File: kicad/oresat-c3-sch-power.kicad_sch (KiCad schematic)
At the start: 67 parts, among them U31 LP2985AIM5-3.3, U34 TPS259621DDA, U35 TPS259620DDA, U36 LTC3624-5, U38 LP2985AIM5-3.3, U6 LTC3624-5

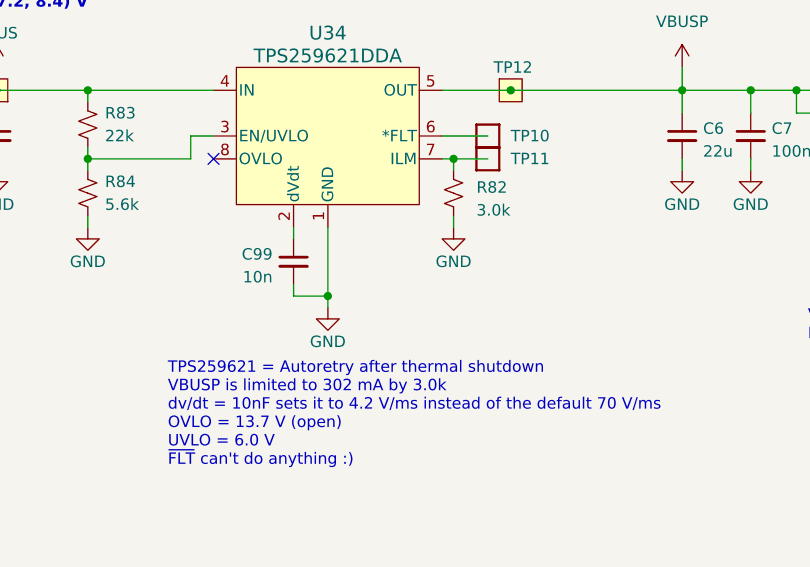
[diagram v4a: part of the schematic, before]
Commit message: Fixed R82 so that the damn thing doesn't reboot every two seconds. Fixed R63 to extend the watchdog timer. Fixed R83 and R84 in order to set the UVLO correctly.
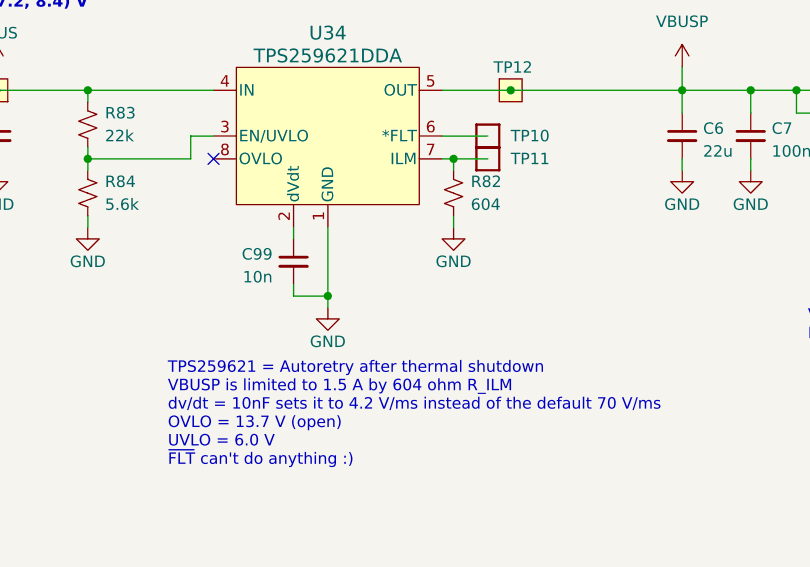
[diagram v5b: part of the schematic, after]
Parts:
- R82: value 3.0k -> 604
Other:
- note added: "TPS259621 = Autoretry after thermal shutdown VBUSP is limited to 1.5 A by 604 ohm R_ILM dv/dt = 10nF sets it to 4.2 V/ms instead of the default 70 V/ms OVLO = 13.7 V (open) UVLO = 6.0 V ~{FLT} can't do anything :)"
- note removed: "TPS259621 = Autoretry after thermal shutdown VBUSP is limited to 302 mA by 3.0k dv/dt = 10nF sets it to 4.2 V/ms instead of the default 70 V/ms OVLO = 13.7 V (open) UVLO = 6.0 V ~{FLT} can't do anything :)"
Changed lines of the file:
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@@
     (effects (font (size 1.27 1.27)) (justify left bottom))
   )
-  (text "TPS259621 = Autoretry after thermal shutdown\nVBUSP is limited to 302 mA by 3.0k\ndv/dt = 10nF sets it to 4.2 V/ms instead of the default 70 V/ms\nOVLO = 13.7 V (open)\nUVLO = 6.0 V\n~{FLT} can't do anything :)"
+  (text "TPS259621 = Autoretry after thermal shutdown\nVBUSP is limited to 1.5 A by 604 ohm R_ILM\ndv/dt = 10nF sets it to 4.2 V/ms instead of the default 70 V/ms\nOVLO = 13.7 V (open)\nUVLO = 6.0 V\n~{FLT} can't do anything :)"
     (at 132.715 114.3 0)
     (effects (font (size 1.27 1.27)) (justify left bottom))
@@
   (symbol (lib_id "Device:R_Small_US") (at 164.465 83.82 0) (unit 1)
     (in_bom yes) (on_board yes) (dnp no) (fields_autoplaced)
-    (property "Reference" "R82" (at 167.005 83.185 0)
-      (effects (font (size 1.27 1.27)) (justify left))
-    )
-    (property "Value" "3.0k" (at 167.005 85.725 0)
-      (effects (font (size 1.27 1.27)) (justify left))
-    )
+    (property "Reference" "R82" (at 166.37 82.55 0)
+      (effects (font (size 1.27 1.27)) (justify left))
+    )
+    (property "Value" "604" (at 166.37 85.09 0)
+      (effects (font (size 1.27 1.27)) (justify left))
+    )

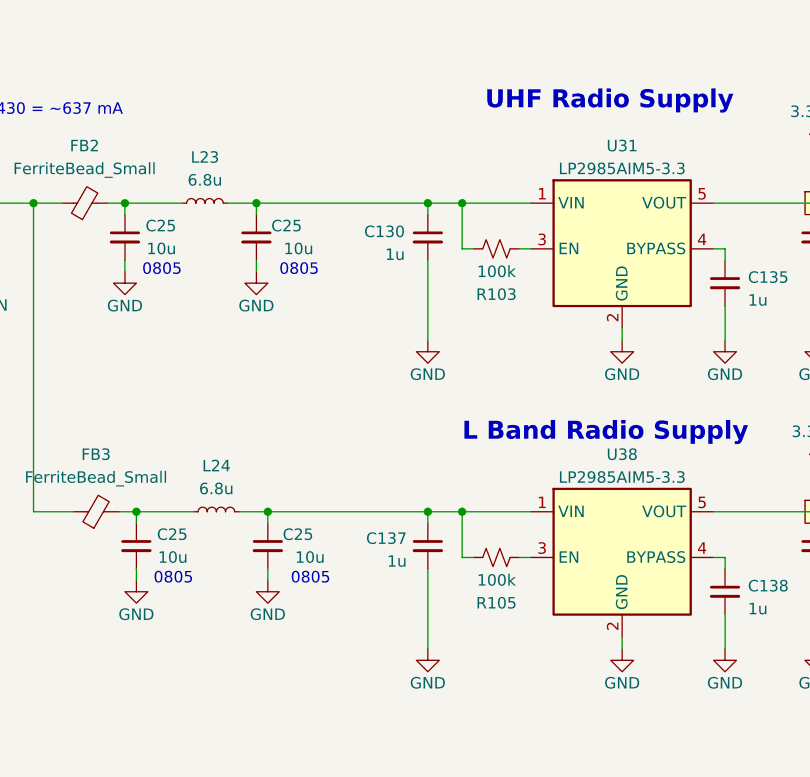
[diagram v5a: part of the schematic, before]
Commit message: changed R values, connected radio enables, more 6.1 implementations
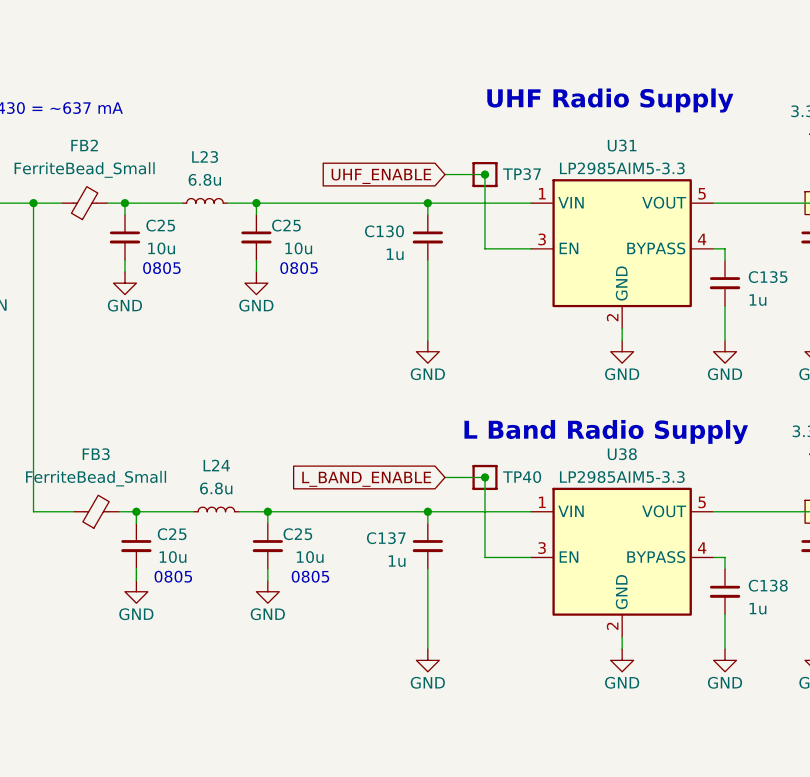
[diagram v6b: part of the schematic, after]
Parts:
- removed R103, R105: 100k, Resistor_SMD:R_0603_1608Metric, symbol Device:R_Small_US
- added TP37, TP40: Test-Point, oresat-misc:TestPoint_Pad_D1.0mm, symbol oresat-misc:Test-Point-1mm-round
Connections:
- net UHF_ENABLE: now reaches U31.3 (EN)
- net UHF_ENABLE: now also TP37.1
- net L_BAND_ENABLE: now reaches U38.3 (EN)
- net L_BAND_ENABLE: now also TP40.1
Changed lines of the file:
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@@
     (title "OreSat C3: Power")
     (date "2023-05-29")
-    (rev "6.0")
+    (rev "6.1")
   )
   (junction (at 349.25 152.4) (diameter 0) (color 0 0 0 0)
@@
   (junction (at 126.365 157.48) (diameter 0) (color 0 0 0 0)
   )
+  (junction (at 312.42 182.88) (diameter 0) (color 0 0 0 0)
+  )
+  (junction (at 312.42 149.225) (diameter 0) (color 0 0 0 0)
+  )
   (junction (at 254.635 72.39) (diameter 0) (color 0 0 0 0)
   )
@@
   (junction (at 349.25 186.69) (diameter 0) (color 0 0 0 0)
   )
-  (junction (at 309.88 186.69) (diameter 0) (color 0 0 0 0)
-  )
   (junction (at 272.415 152.4) (diameter 0) (color 0 0 0 0)
   )
@@
   (junction (at 250.825 152.4) (diameter 0) (color 0 0 0 0)
   )
-  (junction (at 309.88 152.4) (diameter 0) (color 0 0 0 0)
-  )
   (junction (at 113.665 72.39) (diameter 0) (color 0 0 0 0)
   )
@@
     (stroke (width 0) (type default))
   )
+  (wire (pts (xy 307.975 182.88) (xy 312.42 182.88))
+    (stroke (width 0) (type default))
+  )
   (wire (pts (xy 150.495 87.63) (xy 150.495 95.25))
     (stroke (width 0) (type default))
@@
     (stroke (width 0) (type default))
   )
-  (wire (pts (xy 309.88 191.77) (xy 311.15 191.77))
-    (stroke (width 0) (type default))
-  )
   (wire (pts (xy 272.415 80.01) (xy 272.415 82.55))
     (stroke (width 0) (type default))
@@
     (stroke (width 0) (type default))
   )
-  (wire (pts (xy 309.88 186.69) (xy 309.88 191.77))
-    (stroke (width 0) (type default))
-  )
   (wire (pts (xy 75.565 157.48) (xy 79.375 157.48))
     (stroke (width 0) (type default))
@@
     (stroke (width 0) (type default))
   )
-  (wire (pts (xy 309.88 152.4) (xy 306.07 152.4))
-    (stroke (width 0) (type default))
-  )
   (wire (pts (xy 75.565 175.26) (xy 75.565 176.53))
     (stroke (width 0) (type default))
@@
     (stroke (width 0) (type default))
   )
+  (wire (pts (xy 312.42 191.77) (xy 312.42 182.88))
+    (stroke (width 0) (type default))
+  )
   (wire (pts (xy 177.165 152.4) (xy 174.625 152.4))
     (stroke (width 0) (type default))
@@
     (stroke (width 0) (type default))
   )
-  (wire (pts (xy 311.15 157.48) (xy 309.88 157.48))
-    (stroke (width 0) (type default))
-  )
   (wire (pts (xy 272.415 69.85) (xy 272.415 72.39))
     (stroke (width 0) (type default))
@@
     (stroke (width 0) (type default))
   )
-  (wire (pts (xy 317.5 157.48) (xy 316.23 157.48))
+  (wire (pts (xy 312.42 157.48) (xy 317.5 157.48))
     (stroke (width 0) (type default))
   )
@@
     (stroke (width 0) (type default))
   )
+  (wire (pts (xy 307.975 149.225) (xy 312.42 149.225))
+    (stroke (width 0) (type default))
+  )
   (wire (pts (xy 339.09 167.64) (xy 339.09 163.83))
     (stroke (width 0) (type default))
@@
     (stroke (width 0) (type default))
   )
-  (wire (pts (xy 309.88 152.4) (xy 317.5 152.4))
+  (wire (pts (xy 306.07 152.4) (xy 317.5 152.4))
     (stroke (width 0) (type default))
   )
@@
     (stroke (width 0) (type default))
   )
+  (wire (pts (xy 312.42 157.48) (xy 312.42 149.225))
+    (stroke (width 0) (type default))
+  )
   (wire (pts (xy 263.525 72.39) (xy 272.415 72.39))
     (stroke (width 0) (type default))
@@
     (stroke (width 0) (type default))
   )
-  (wire (pts (xy 317.5 191.77) (xy 316.23 191.77))
+  (wire (pts (xy 312.42 191.77) (xy 317.5 191.77))
     (stroke (width 0) (type default))
   )
@@
     (stroke (width 0) (type default))
   )
-  (wire (pts (xy 306.07 186.69) (xy 309.88 186.69))
-    (stroke (width 0) (type default))
-  )
-  (wire (pts (xy 309.88 157.48) (xy 309.88 152.4))
-    (stroke (width 0) (type default))
-  )
   (wire (pts (xy 240.665 146.05) (xy 240.665 152.4))
     (stroke (width 0) (type default))
@@
     (stroke (width 0) (type default))
   )
-  (wire (pts (xy 317.5 186.69) (xy 309.88 186.69))
+  (wire (pts (xy 306.07 186.69) (xy 317.5 186.69))
     (stroke (width 0) (type default))
   )
@@
     )
   )
+  (global_label "UHF_ENABLE" (shape input) (at 307.975 149.225 180) (fields_autoplaced)
+    (effects (font (size 1.27 1.27)) (justify right))
+    (property "Intersheetrefs" "${INTERSHEET_REFS}" (at 293.2574 149.225 0)
+      (effects (font (size 1.27 1.27)) (justify right))
+    )
+  )
+  (global_label "L_BAND_ENABLE" (shape input) (at 307.975 182.88 180) (fields_autoplaced)
+    (effects (font (size 1.27 1.27)) (justify right))
+    (property "Intersheetrefs" "${INTERSHEET_REFS}" (at 290.0522 182.88 0)
+      (effects (font (size 1.27 1.27)) (justify right))
+    )
+  )
   (symbol (lib_id "power:GND") (at 161.925 160.02 0) (unit 1)
     (in_bom yes) (on_board yes) (dnp no)
@@
     )
   )
-  (symbol (lib_id "Device:R_Small_US") (at 313.69 157.48 90) (unit 1)
-    (in_bom yes) (on_board yes) (dnp no)
-    (property "Reference" "R103" (at 313.69 162.56 90)
-      (effects (font (size 1.27 1.27)))
-    )
-    (property "Value" "100k" (at 313.69 160.02 90)
-      (effects (font (size 1.27 1.27)))
-    )
-    (property "Footprint" "Resistor_SMD:R_0603_1608Metric" (at 313.69 157.48 0)
-      (effects (font (size 1.27 1.27)) hide)
-    )
-    (property "Datasheet" "~" (at 313.69 157.48 0)
-      (effects (font (size 1.27 1.27)) hide)
-    )
-    (pin "1")
-    (pin "2")
-    (instances
-      (project "oresat-c3"
-        (path "/65d12cdd-c326-4033-9053-c59fa4e0b25e/2134bb9a-062c-4e32-a41e-d15ce3545372"
-          (reference "R103") (unit 1)
-        )
-      )
-    )
-  )
   (symbol (lib_id "power:GND") (at 349.25 201.93 0) (unit 1)
     (in_bom yes) (on_board yes) (dnp no)
@@
     )
   )
-  (symbol (lib_id "Device:R_Small_US") (at 313.69 191.77 90) (unit 1)
-    (in_bom yes) (on_board yes) (dnp no)
-    (property "Reference" "R105" (at 313.69 196.85 90)
-      (effects (font (size 1.27 1.27)))
-    )
-    (property "Value" "100k" (at 313.69 194.31 90)
-      (effects (font (size 1.27 1.27)))
-    )
-    (property "Footprint" "Resistor_SMD:R_0603_1608Metric" (at 313.69 191.77 0)
-      (effects (font (size 1.27 1.27)) hide)
-    )
-    (property "Datasheet" "~" (at 313.69 191.77 0)
-      (effects (font (size 1.27 1.27)) hide)
-    )
-    (pin "1")
-    (pin "2")
-    (instances
-      (project "oresat-c3"
-        (path "/65d12cdd-c326-4033-9053-c59fa4e0b25e/2134bb9a-062c-4e32-a41e-d15ce3545372"
-          (reference "R105") (unit 1)
-        )
-      )
-    )
-  )
   (symbol (lib_id "Device:FerriteBead_Small") (at 267.97 152.4 90) (unit 1)
     (in_bom yes) (on_board yes) (dnp no) (fields_autoplaced)
@@
     )
   )
+  (symbol (lib_id "oresat-misc:Test-Point-1mm-round") (at 312.42 182.88 180) (unit 1)
+    (in_bom yes) (on_board yes) (dnp no)
+    (property "Reference" "TP40" (at 318.77 182.88 0)
+      (effects (font (size 1.27 1.27)) (justify left))
+    )
+    (property "Value" "Test-Point" (at 312.42 185.42 0)
+      (effects (font (size 1.27 1.27)) hide)
+    )
+    (property "Footprint" "oresat-misc:TestPoint_Pad_D1.0mm" (at 312.42 193.04 0)
+      (effects (font (size 1.27 1.27)) hide)
+    )
+    (property "Datasheet" "" (at 312.42 182.88 0)
+      (effects (font (size 1.27 1.27)) hide)
+    )
+    (pin "1")
+    (instances
+      (project "oresat-c3"
+        (path "/65d12cdd-c326-4033-9053-c59fa4e0b25e/f3d147ad-4cea-4d77-ae60-95882b03454e"
+          (reference "TP40") (unit 1)
+        )
+        (path "/65d12cdd-c326-4033-9053-c59fa4e0b25e/2134bb9a-062c-4e32-a41e-d15ce3545372"
+          (reference "TP40") (unit 1)
+        )
+      )
+    )
+  )
   (symbol (lib_id "power:GND") (at 164.465 87.63 0) (unit 1)
     (in_bom yes) (on_board yes) (dnp no)
@@
         )
       )
+    )
+  )
+  (symbol (lib_id "oresat-misc:Test-Point-1mm-round") (at 312.42 149.225 180) (unit 1)
+    (in_bom yes) (on_board yes) (dnp no)
+    (property "Reference" "TP37" (at 318.77 149.225 0)
+      (effects (font (size 1.27 1.27)) (justify left))
+    )
+    (property "Value" "Test-Point" (at 312.42 151.765 0)
+      (effects (font (size 1.27 1.27)) hide)
+    )
+    (property "Footprint" "oresat-misc:TestPoint_Pad_D1.0mm" (at 312.42 159.385 0)
+      (effects (font (size 1.27 1.27)) hide)
+    )
+    (property "Datasheet" "" (at 312.42 149.225 0)
+      (effects (font (size 1.27 1.27)) hide)
+    )
+    (pin "1")
+    (instances
+      (project "oresat-c3"
+        (path "/65d12cdd-c326-4033-9053-c59fa4e0b25e/f3d147ad-4cea-4d77-ae60-95882b03454e"
+          (reference "TP37") (unit 1)
+        )
+        (path "/65d12cdd-c326-4033-9053-c59fa4e0b25e/2134bb9a-062c-4e32-a41e-d15ce3545372"
+          (reference "TP37") (unit 1)
+        )
+      )

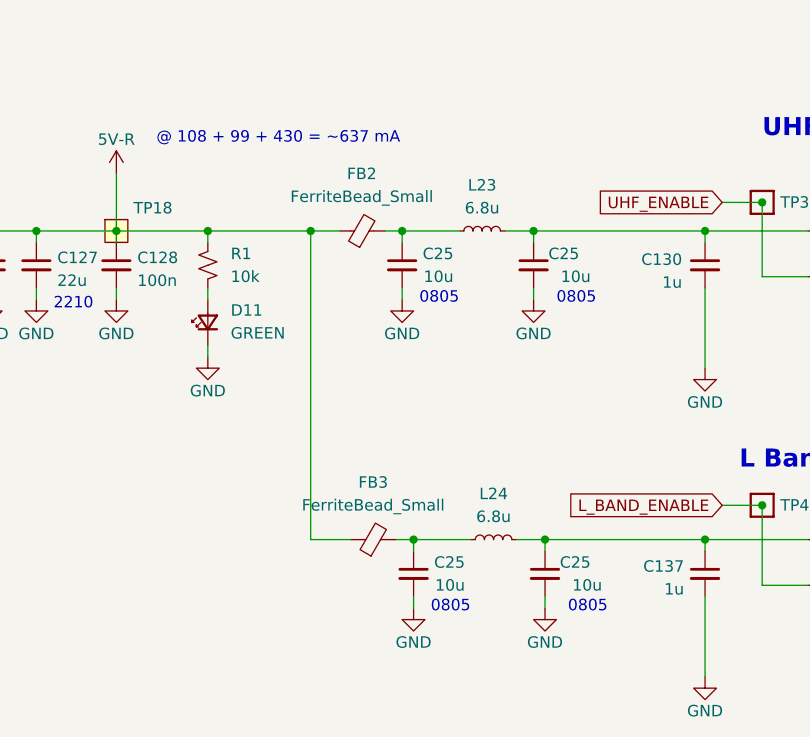
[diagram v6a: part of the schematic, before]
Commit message: Real part numbers for FB parts, routed signals for the UHF_ENABLE AND L_BAND_ENABLE signals.
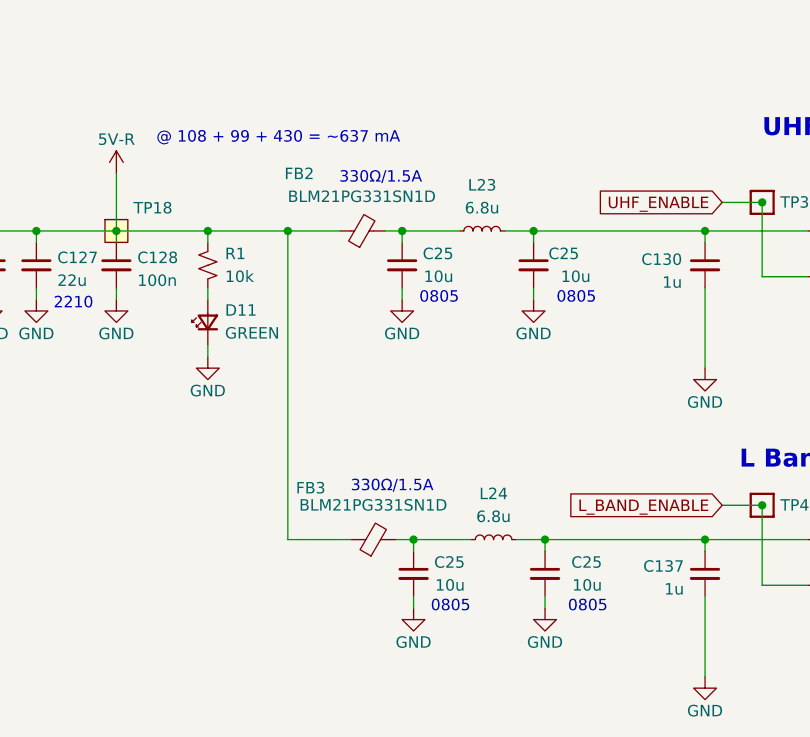
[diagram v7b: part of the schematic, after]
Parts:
- FB2, FB3: value FerriteBead_Small -> BLM21PG331SN1D
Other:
- note added: "330Ω/1.5A"
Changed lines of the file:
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@@
   (junction (at 113.665 152.4) (diameter 0) (color 0 0 0 0)
   )
-  (junction (at 262.255 152.4) (diameter 0) (color 0 0 0 0)
+  (junction (at 259.715 152.4) (diameter 0) (color 0 0 0 0)
   )
   (junction (at 109.855 160.02) (diameter 0) (color 0 0 0 0)
@@
     (stroke (width 0) (type default))
   )
-  (wire (pts (xy 262.255 152.4) (xy 265.43 152.4))
+  (wire (pts (xy 259.715 152.4) (xy 265.43 152.4))
     (stroke (width 0) (type default))
   )
@@
     (stroke (width 0) (type default))
   )
-  (wire (pts (xy 262.255 152.4) (xy 262.255 186.69))
+  (wire (pts (xy 259.715 152.4) (xy 259.715 186.69))
     (stroke (width 0) (type default))
   )
@@
     (stroke (width 0) (type default))
   )
-  (wire (pts (xy 250.825 152.4) (xy 262.255 152.4))
+  (wire (pts (xy 250.825 152.4) (xy 259.715 152.4))
     (stroke (width 0) (type default))
   )
@@
     (stroke (width 0) (type default))
   )
-  (wire (pts (xy 266.7 186.69) (xy 262.255 186.69))
+  (wire (pts (xy 266.7 186.69) (xy 259.715 186.69))
     (stroke (width 0) (type default))
   )
@@
   (wire (pts (xy 337.82 157.48) (xy 339.09 157.48))
     (stroke (width 0) (type default))
+  )
+  (text "330Ω/1.5A" (at 265.43 147.32 0)
+    (effects (font (size 1.27 1.27)) (justify left bottom))
   )
   (text "@ ~99 mA (150 mA max) = 168 mW" (at 354.965 178.435 0)
@@
   )
   (text "0805" (at 289.56 160.655 0)
+    (effects (font (size 1.27 1.27)) (justify left bottom))
+  )
+  (text "330Ω/1.5A" (at 266.7 181.61 0)
     (effects (font (size 1.27 1.27)) (justify left bottom))
   )
@@
   )
   (symbol (lib_id "Device:LED_Small") (at 250.825 162.56 90) (unit 1)
-    (in_bom yes) (on_board yes) (dnp no) (fields_autoplaced)
-    (property "Reference" "D11" (at 253.365 161.2264 90)
+    (in_bom yes) (on_board yes) (dnp no)
+    (property "Reference" "D11" (at 252.73 161.2264 90)
       (effects (font (size 1.27 1.27)) (justify right))
     )
-    (property "Value" "GREEN" (at 253.365 163.7664 90)
+    (property "Value" "GREEN" (at 252.73 163.7664 90)
       (effects (font (size 1.27 1.27)) (justify right))
     )
@@
   )
   (symbol (lib_id "Device:FerriteBead_Small") (at 267.97 152.4 90) (unit 1)
-    (in_bom yes) (on_board yes) (dnp no) (fields_autoplaced)
-    (property "Reference" "FB2" (at 267.9319 146.05 90)
-      (effects (font (size 1.27 1.27)))
-    )
-    (property "Value" "FerriteBead_Small" (at 267.9319 148.59 90)
+    (in_bom yes) (on_board yes) (dnp no)
+    (property "Reference" "FB2" (at 260.985 146.05 90)
+      (effects (font (size 1.27 1.27)))
+    )
+    (property "Value" "BLM21PG331SN1D" (at 267.9319 148.59 90)
       (effects (font (size 1.27 1.27)))
     )
@@
   (symbol (lib_id "Device:C_Small") (at 288.29 190.5 0) (mirror y) (unit 1)
     (in_bom yes) (on_board yes) (dnp no)
-    (property "Reference" "C25" (at 293.37 189.23 0)
+    (property "Reference" "C25" (at 294.64 189.23 0)
       (effects (font (size 1.27 1.27)) (justify left))
     )
@@
   )
   (symbol (lib_id "Device:FerriteBead_Small") (at 269.24 186.69 90) (unit 1)
-    (in_bom yes) (on_board yes) (dnp no) (fields_autoplaced)
-    (property "Reference" "FB3" (at 269.2019 180.34 90)
-      (effects (font (size 1.27 1.27)))
-    )
-    (property "Value" "FerriteBead_Small" (at 269.2019 182.88 90)
+    (in_bom yes) (on_board yes) (dnp no)
+    (property "Reference" "FB3" (at 262.255 180.975 90)
+      (effects (font (size 1.27 1.27)))
+    )
+    (property "Value" "BLM21PG331SN1D" (at 269.2019 182.88 90)
       (effects (font (size 1.27 1.27)))
     )
@@
   (symbol (lib_id "Device:R_Small_US") (at 250.825 156.21 0) (mirror x) (unit 1)
     (in_bom yes) (on_board yes) (dnp no)
-    (property "Reference" "R1" (at 253.365 154.94 0)
-      (effects (font (size 1.27 1.27)) (justify left))
-    )
-    (property "Value" "10k" (at 253.365 157.48 0)
-      (effects (font (size 1.27 1.27)) (justify left))
-    )
+    (property "Reference" "R1" (at 252.73 154.94 0)
+      (effects (font (size 1.27 1.27)) (justify left))
+    )
+    (property "Value" "10k" (at 252.73 157.48 0)
+      (effects (font (size 1.27 1.27)) (justify left))
+    )
